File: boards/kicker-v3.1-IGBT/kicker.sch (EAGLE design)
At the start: 132 parts, among them J1 B2PS-VH(LF)(SN), J2 HFW8R-1ST, J3 B2PS-VH(LF)(SN), J4 B2PS-VH(LF)(SN), J5 2-PIN_2MM-H, J6 3-PIN_2MM-H, J7 !BTN_KCK_PRE_EXT, J8 !BTN_CHP_PRE_EXT, J9 !BTN_CHG_PRE_EXT, Q1 ATP302ATPAK, Q10 BSS806NSOT-23-3, Q2 IRFS4227, Q3 BSS127, Q4 BSS127, Q5 BSS127, Q6 BSS127, Q7 AOD1N60, U1 R-78E5.0-0.5, U2 15V, U3 LT3751FE, U4 AT32ATQFP44, U5 IX4427N, U6 MAX6817, U7 MAX6817

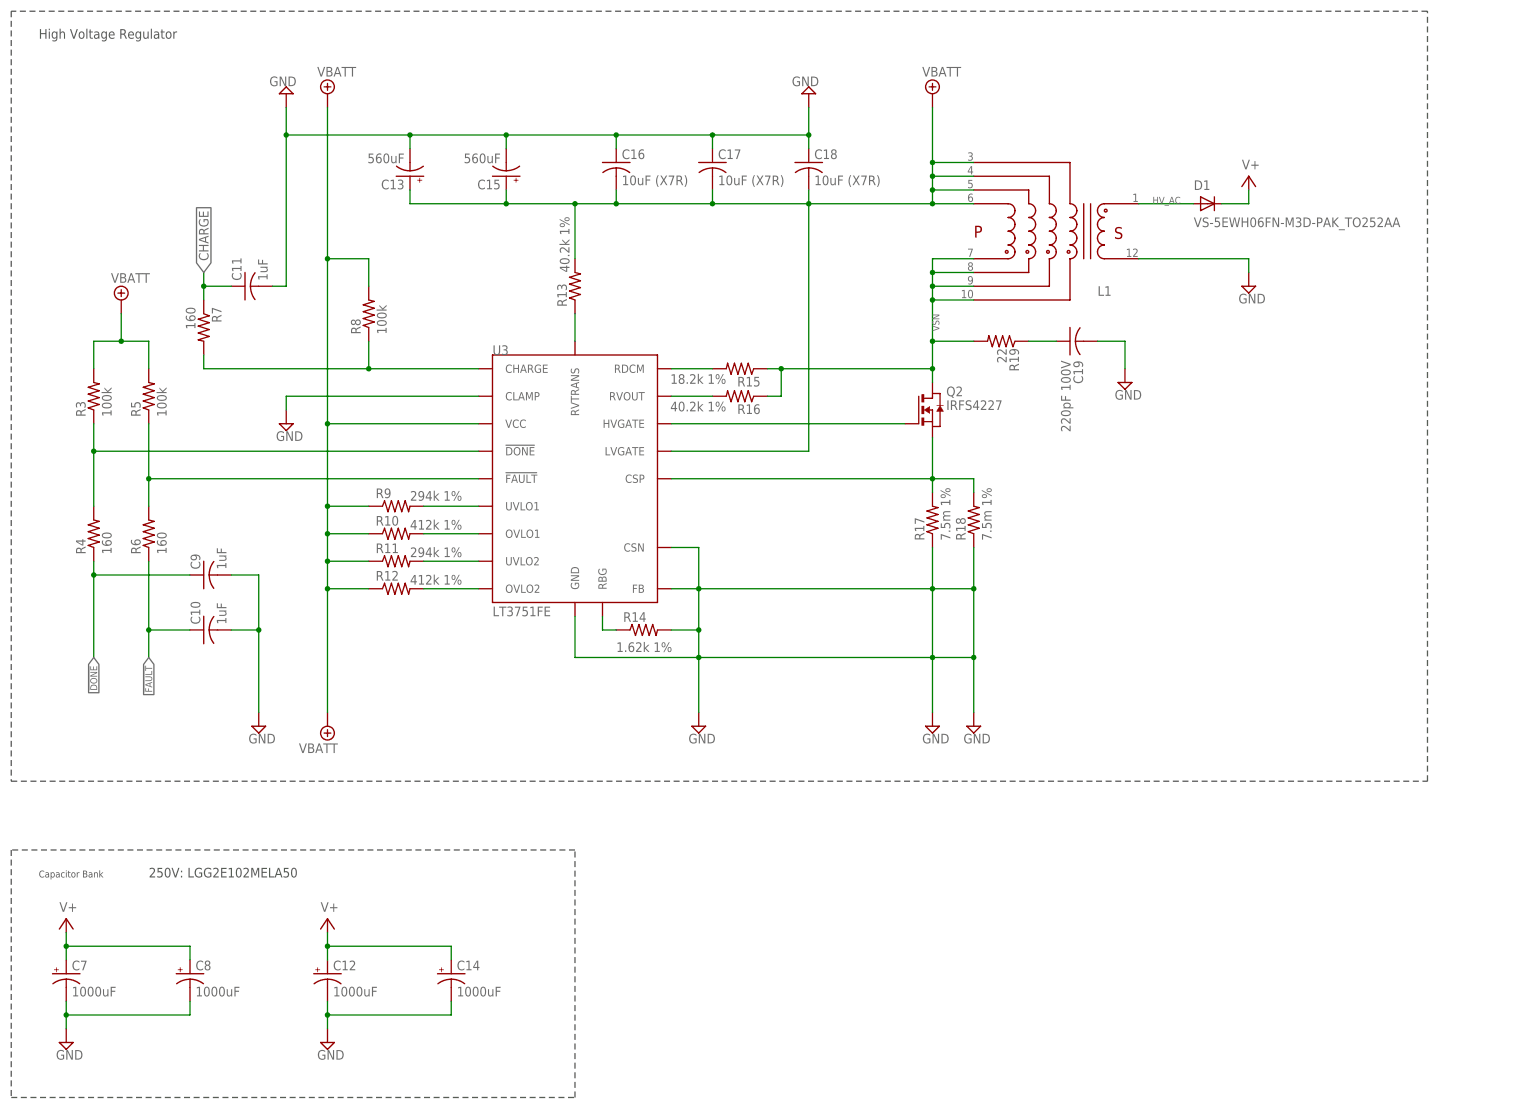
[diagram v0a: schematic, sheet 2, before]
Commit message: fixes to pull ups and added tvs diode(vbatt)
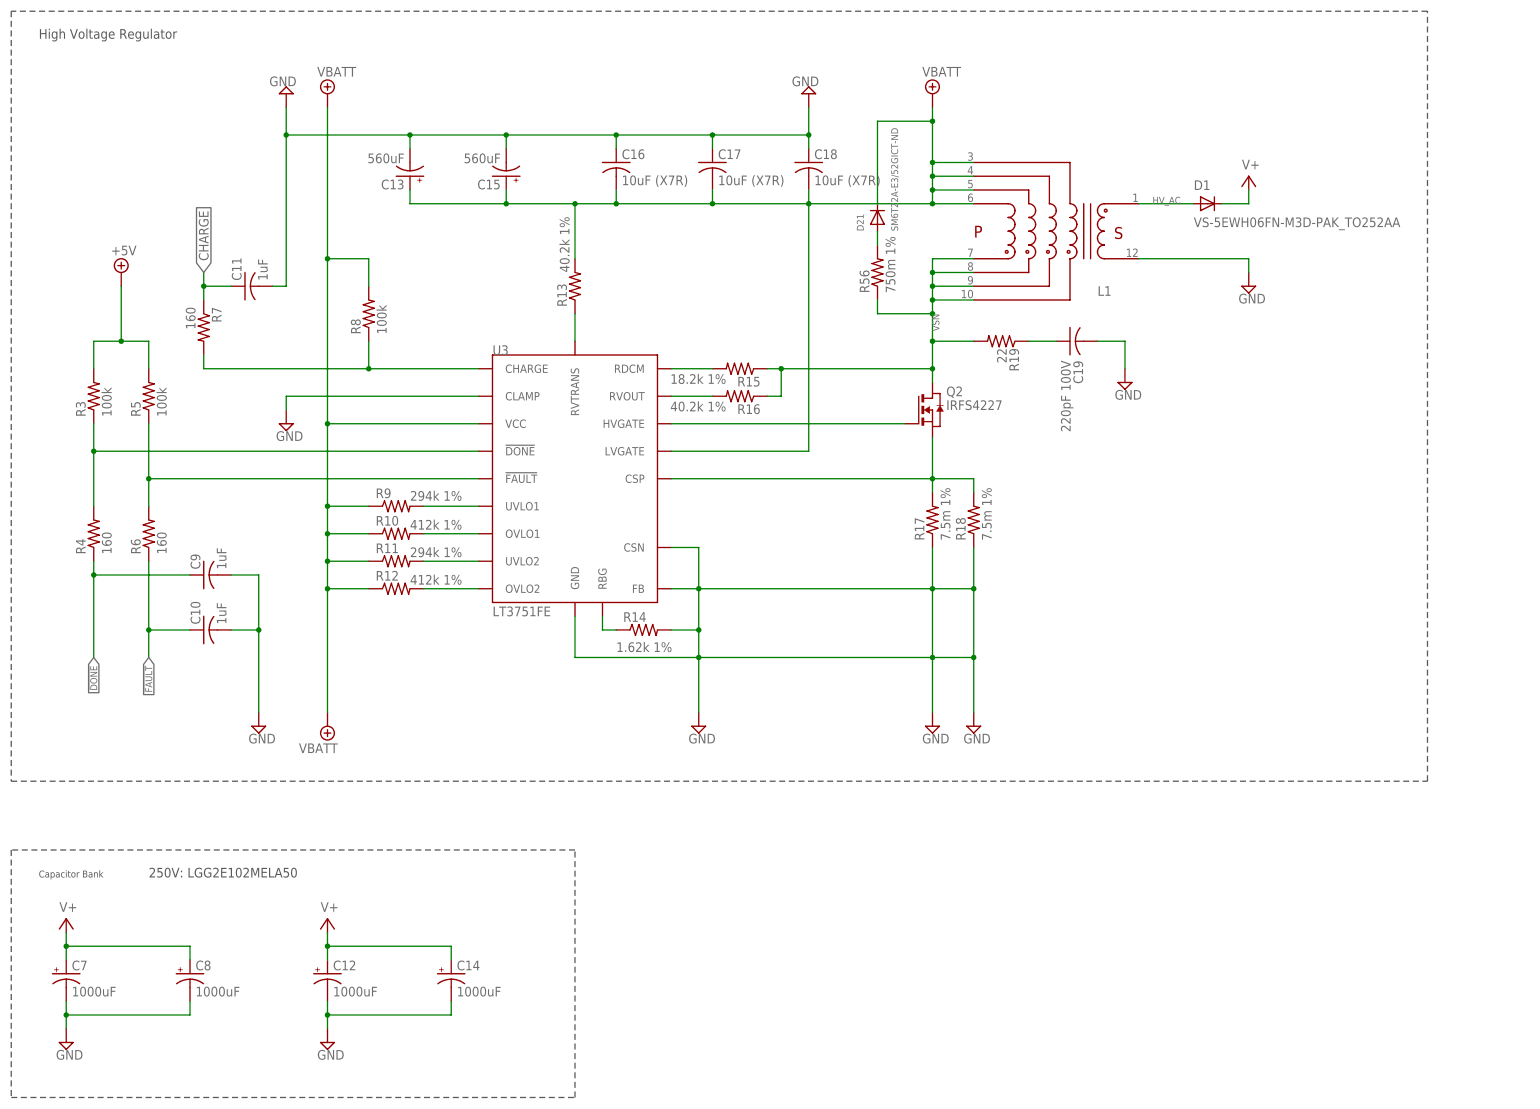
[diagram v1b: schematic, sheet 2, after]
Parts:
- added D21: SM6T22A-E3/52GICT-ND, adafruit:DIODESOD-123
- added R56: 750m 1%, resistor:R-US_M0805
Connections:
- new net N$23: D21.A, R56.2
- net +5V: now also R3.2, R5.2
- net VBATT: now also D21.C; no longer R3.2, R5.2
- net VSN: now also R56.1

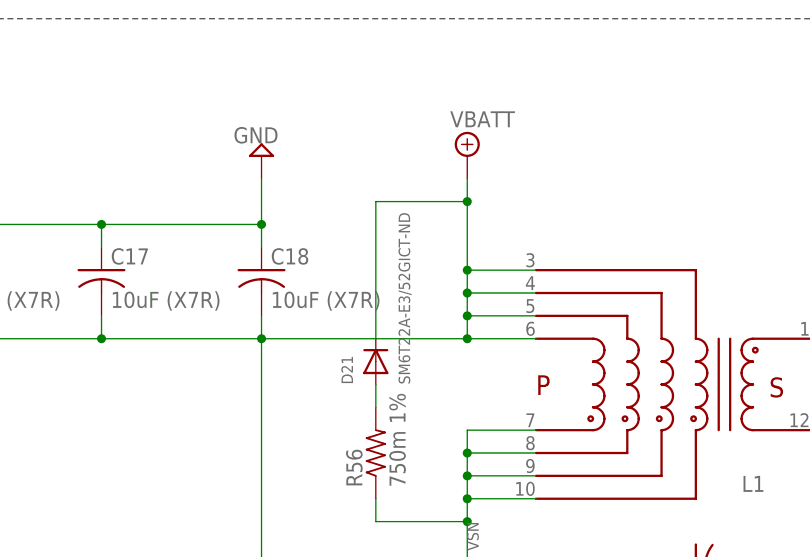
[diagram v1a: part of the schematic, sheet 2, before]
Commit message: Changed TVS Diode
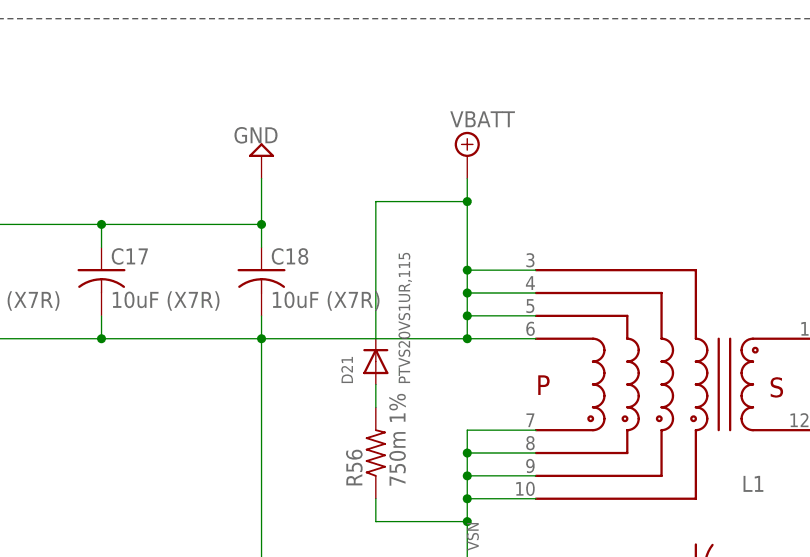
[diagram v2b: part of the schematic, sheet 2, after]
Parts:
- D21: value SM6T22A-E3/52GICT-ND -> PTVS20VS1UR,115
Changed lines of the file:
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@@
 <grid distance="0.1" unitdist="inch" unit="inch" style="lines" multiple="1" display="no" altdistance="0.01" altunitdist="inch" altunit="inch"/>
 <layers>
-<layer number="1" name="Top" color="4" fill="1" visible="yes" active="no"/>
-<layer number="2" name="Route2" color="1" fill="3" visible="yes" active="no"/>
-<layer number="3" name="Route3" color="4" fill="3" visible="yes" active="no"/>
-<layer number="4" name="Route4" color="1" fill="4" visible="yes" active="no"/>
-<layer number="5" name="Route5" color="4" fill="4" visible="yes" active="no"/>
-<layer number="6" name="Route6" color="1" fill="8" visible="yes" active="no"/>
-<layer number="7" name="Route7" color="4" fill="8" visible="yes" active="no"/>
-<layer number="8" name="Route8" color="1" fill="2" visible="yes" active="no"/>
-<layer number="9" name="Route9" color="4" fill="2" visible="yes" active="no"/>
-<layer number="10" name="Route10" color="1" fill="7" visible="yes" active="no"/>
-<layer number="11" name="Route11" color="4" fill="7" visible="yes" active="no"/>
-<layer number="12" name="Route12" color="1" fill="5" visible="yes" active="no"/>
-<layer number="13" name="Route13" color="4" fill="5" visible="yes" active="no"/>
-<layer number="14" name="Route14" color="1" fill="6" visible="yes" active="no"/>
-<layer number="15" name="Route15" color="4" fill="6" visible="yes" active="no"/>
-<layer number="16" name="Bottom" color="1" fill="1" visible="yes" active="no"/>
-<layer number="17" name="Pads" color="2" fill="1" visible="yes" active="no"/>
-<layer number="18" name="Vias" color="2" fill="1" visible="yes" active="no"/>
-<layer number="19" name="Unrouted" color="6" fill="1" visible="yes" active="no"/>
-<layer number="20" name="Dimension" color="15" fill="1" visible="yes" active="no"/>
-<layer number="21" name="tPlace" color="7" fill="1" visible="yes" active="no"/>
-<layer number="22" name="bPlace" color="7" fill="1" visible="yes" active="no"/>
-<layer number="23" name="tOrigins" color="15" fill="1" visible="yes" active="no"/>
-<layer number="24" name="bOrigins" color="15" fill="1" visible="yes" active="no"/>
-<layer number="25" name="tNames" color="7" fill="1" visible="yes" active="no"/>
-<layer number="26" name="bNames" color="7" fill="1" visible="yes" active="no"/>
-<layer number="27" name="tValues" color="7" fill="1" visible="yes" active="no"/>
-<layer number="28" name="bValues" color="7" fill="1" visible="yes" active="no"/>
+<layer number="1" name="Top" color="4" fill="1" visible="no" active="no"/>
+<layer number="2" name="Route2" color="1" fill="3" visible="no" active="no"/>
+<layer number="3" name="Route3" color="4" fill="3" visible="no" active="no"/>
+<layer number="4" name="Route4" color="1" fill="4" visible="no" active="no"/>
+<layer number="5" name="Route5" color="4" fill="4" visible="no" active="no"/>
+<layer number="6" name="Route6" color="1" fill="8" visible="no" active="no"/>
+<layer number="7" name="Route7" color="4" fill="8" visible="no" active="no"/>
+<layer number="8" name="Route8" color="1" fill="2" visible="no" active="no"/>
+<layer number="9" name="Route9" color="4" fill="2" visible="no" active="no"/>
+<layer number="10" name="Route10" color="1" fill="7" visible="no" active="no"/>
+<layer number="11" name="Route11" color="4" fill="7" visible="no" active="no"/>
+<layer number="12" name="Route12" color="1" fill="5" visible="no" active="no"/>
+<layer number="13" name="Route13" color="4" fill="5" visible="no" active="no"/>
+<layer number="14" name="Route14" color="1" fill="6" visible="no" active="no"/>
+<layer number="15" name="Route15" color="4" fill="6" visible="no" active="no"/>
+<layer number="16" name="Bottom" color="1" fill="1" visible="no" active="no"/>
+<layer number="17" name="Pads" color="2" fill="1" visible="no" active="no"/>
+<layer number="18" name="Vias" color="2" fill="1" visible="no" active="no"/>
+<layer number="19" name="Unrouted" color="6" fill="1" visible="no" active="no"/>
+<layer number="20" name="Dimension" color="15" fill="1" visible="no" active="no"/>
+<layer number="21" name="tPlace" color="7" fill="1" visible="no" active="no"/>
+<layer number="22" name="bPlace" color="7" fill="1" visible="no" active="no"/>
+<layer number="23" name="tOrigins" color="15" fill="1" visible="no" active="no"/>
+<layer number="24" name="bOrigins" color="15" fill="1" visible="no" active="no"/>
+<layer number="25" name="tNames" color="7" fill="1" visible="no" active="no"/>
+<layer number="26" name="bNames" color="7" fill="1" visible="no" active="no"/>
+<layer number="27" name="tValues" color="7" fill="1" visible="no" active="no"/>
+<layer number="28" name="bValues" color="7" fill="1" visible="no" active="no"/>
 <layer number="29" name="tStop" color="7" fill="3" visible="no" active="no"/>
 <layer number="30" name="bStop" color="7" fill="6" visible="no" active="no"/>
@@
 <layer number="35" name="tGlue" color="7" fill="4" visible="no" active="no"/>
 <layer number="36" name="bGlue" color="7" fill="5" visible="no" active="no"/>
-<layer number="37" name="tTest" color="7" fill="1" visible="yes" active="no"/>
-<layer number="38" name="bTest" color="7" fill="1" visible="yes" active="no"/>
+<layer number="37" name="tTest" color="7" fill="1" visible="no" active="no"/>
+<layer number="38" name="bTest" color="7" fill="1" visible="no" active="no"/>
 <layer number="39" name="tKeepout" color="4" fill="11" visible="no" active="no"/>
 <layer number="40" name="bKeepout" color="1" fill="11" visible="no" active="no"/>
@@
 <layer number="44" name="Drills" color="7" fill="1" visible="no" active="no"/>
 <layer number="45" name="Holes" color="7" fill="1" visible="no" active="no"/>
-<layer number="46" name="Milling" color="3" fill="1" visible="yes" active="no"/>
-<layer number="47" name="Measures" color="7" fill="1" visible="yes" active="no"/>
-<layer number="48" name="Document" color="7" fill="1" visible="yes" active="no"/>
-<layer number="49" name="Reference" color="7" fill="1" visible="yes" active="no"/>
-<layer number="50" name="dxf" color="7" fill="1" visible="yes" active="no"/>
-<layer number="51" name="tDocu" color="7" fill="1" visible="yes" active="no"/>
-<layer number="52" name="bDocu" color="7" fill="1" visible="yes" active="no"/>
-<layer number="53" name="tGND_GNDA" color="7" fill="9" visible="yes" active="no"/>
-<layer number="54" name="bGND_GNDA" color="1" fill="9" visible="yes" active="no"/>
-<layer number="56" name="wert" color="7" fill="1" visible="yes" active="no"/>
-<layer number="57" name="tCAD" color="7" fill="1" visible="yes" active="no"/>
-<layer number="59" name="tCarbon" color="7" fill="1" visible="yes" active="no"/>
-<layer number="60" name="bCarbon" color="7" fill="1" visible="yes" active="no"/>
+<layer number="46" name="Milling" color="3" fill="1" visible="no" active="no"/>
+<layer number="47" name="Measures" color="7" fill="1" visible="no" active="no"/>
+<layer number="48" name="Document" color="7" fill="1" visible="no" active="no"/>
+<layer number="49" name="Reference" color="7" fill="1" visible="no" active="no"/>
+<layer number="50" name="dxf" color="7" fill="1" visible="no" active="no"/>
+<layer number="51" name="tDocu" color="7" fill="1" visible="no" active="no"/>
+<layer number="52" name="bDocu" color="7" fill="1" visible="no" active="no"/>
+<layer number="53" name="tGND_GNDA" color="7" fill="9" visible="no" active="no"/>
+<layer number="54" name="bGND_GNDA" color="1" fill="9" visible="no" active="no"/>
+<layer number="56" name="wert" color="7" fill="1" visible="no" active="no"/>
+<layer number="57" name="tCAD" color="7" fill="1" visible="no" active="no"/>
+<layer number="59" name="tCarbon" color="7" fill="1" visible="no" active="no"/>
+<layer number="60" name="bCarbon" color="7" fill="1" visible="no" active="no"/>
 <layer number="90" name="Modules" color="5" fill="1" visible="yes" active="yes"/>
 <layer number="91" name="Nets" color="2" fill="1" visible="yes" active="yes"/>
@@
 <part name="U$6" library="RoboJackets-Discrete" deviceset="IXGK400N30A3" device=""/>
 <part name="U$7" library="RoboJackets-Discrete" deviceset="IXGK400N30A3" device=""/>
-<part name="D21" library="adafruit" deviceset="DIODE" device="SOD-123" value="SM6T22A-E3/52GICT-ND"/>
+<part name="D21" library="adafruit" deviceset="DIODE" device="SOD-123" value="PTVS20VS1UR,115 "/>
 <part name="R56" library="resistor" library_urn="urn:adsk.eagle:library:348" deviceset="R-US_" device="M0805" package3d_urn="urn:adsk.eagle:package:26079/1" value="750m 1%"/>
 <part name="SUPPLY12" library="supply2" library_urn="urn:adsk.eagle:library:372" deviceset="+5V" device=""/>
